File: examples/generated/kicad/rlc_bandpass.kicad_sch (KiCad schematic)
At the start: 5 parts

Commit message: Attempt to create legible symbols.
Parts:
- C1: symbol examples:CAP -> CAP
- L1: symbol examples:INDUCTOR -> INDUCTOR
- R1, R2: symbol examples:R -> R
- V1: symbol examples:VSOURCE -> VSOURCE
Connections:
- net GND: now also C1.1, C1.2, L1.2, R2.1, R2.2, V1.1 (E1)
- new net: R1.1, V1.2 (E2)
- new net: L1.1, R1.2
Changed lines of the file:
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@@
     (comment 1 "Generated by mixedsig2cad")
   )
-  (symbol (lib_id "examples:VSOURCE") (at 50.00 55.00 0) (unit 1)
+  (symbol (lib_id "VSOURCE") (at 50.00 55.00 0) (unit 1)
     (in_bom yes) (on_board yes)
     (property "Reference" "V1" (at 50.0 51.19 0)
@@
     )
   )
-  (symbol (lib_id "examples:R") (at 95.00 55.00 90) (unit 1)
+  (symbol (lib_id "R") (at 95.00 55.00 90) (unit 1)
     (in_bom yes) (on_board yes)
     (property "Reference" "R1" (at 95.0 51.19 0)
@@
     )
   )
-  (symbol (lib_id "examples:INDUCTOR") (at 95.00 90.00 0) (unit 1)
+  (symbol (lib_id "INDUCTOR") (at 95.00 90.00 0) (unit 1)
     (in_bom yes) (on_board yes)
     (property "Reference" "L1" (at 95.0 86.19 0)
@@
     )
   )
-  (symbol (lib_id "examples:CAP") (at 95.00 125.00 90) (unit 1)
+  (symbol (lib_id "CAP") (at 95.00 125.00 90) (unit 1)
     (in_bom yes) (on_board yes)
     (property "Reference" "C1" (at 95.0 121.19 0)
@@
     )
   )
-  (symbol (lib_id "examples:R") (at 95.00 160.00 90) (unit 1)
+  (symbol (lib_id "R") (at 95.00 160.00 90) (unit 1)
     (in_bom yes) (on_board yes)
     (property "Reference" "R2" (at 95.0 156.19 0)
@@
     )
   )
-  (symbol (lib_id "examples:GND") (at 38.00 41.38 0) (unit 1)
+  (symbol (lib_id "GND") (at 38.00 41.38 0) (unit 1)
     (in_bom yes) (on_board yes)
     (property "Reference" "#PWR0001" (at 38.0 37.57 0)

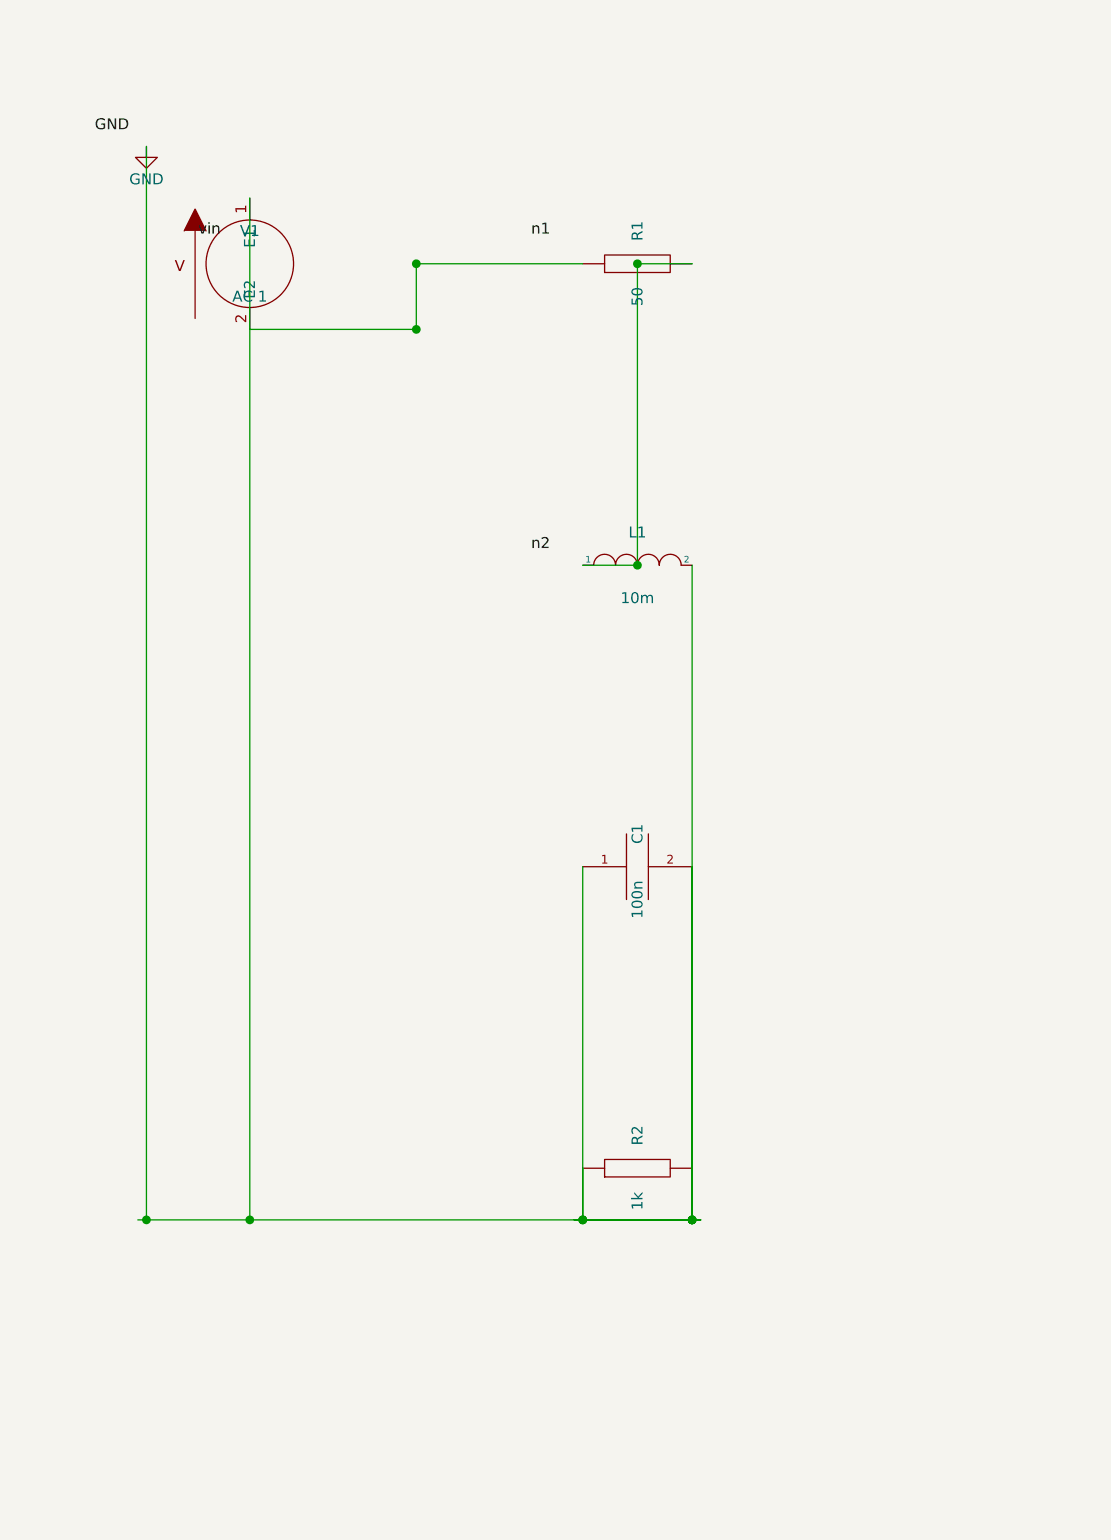
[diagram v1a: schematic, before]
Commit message: Attempt full seperation of circuit concerns into layers.
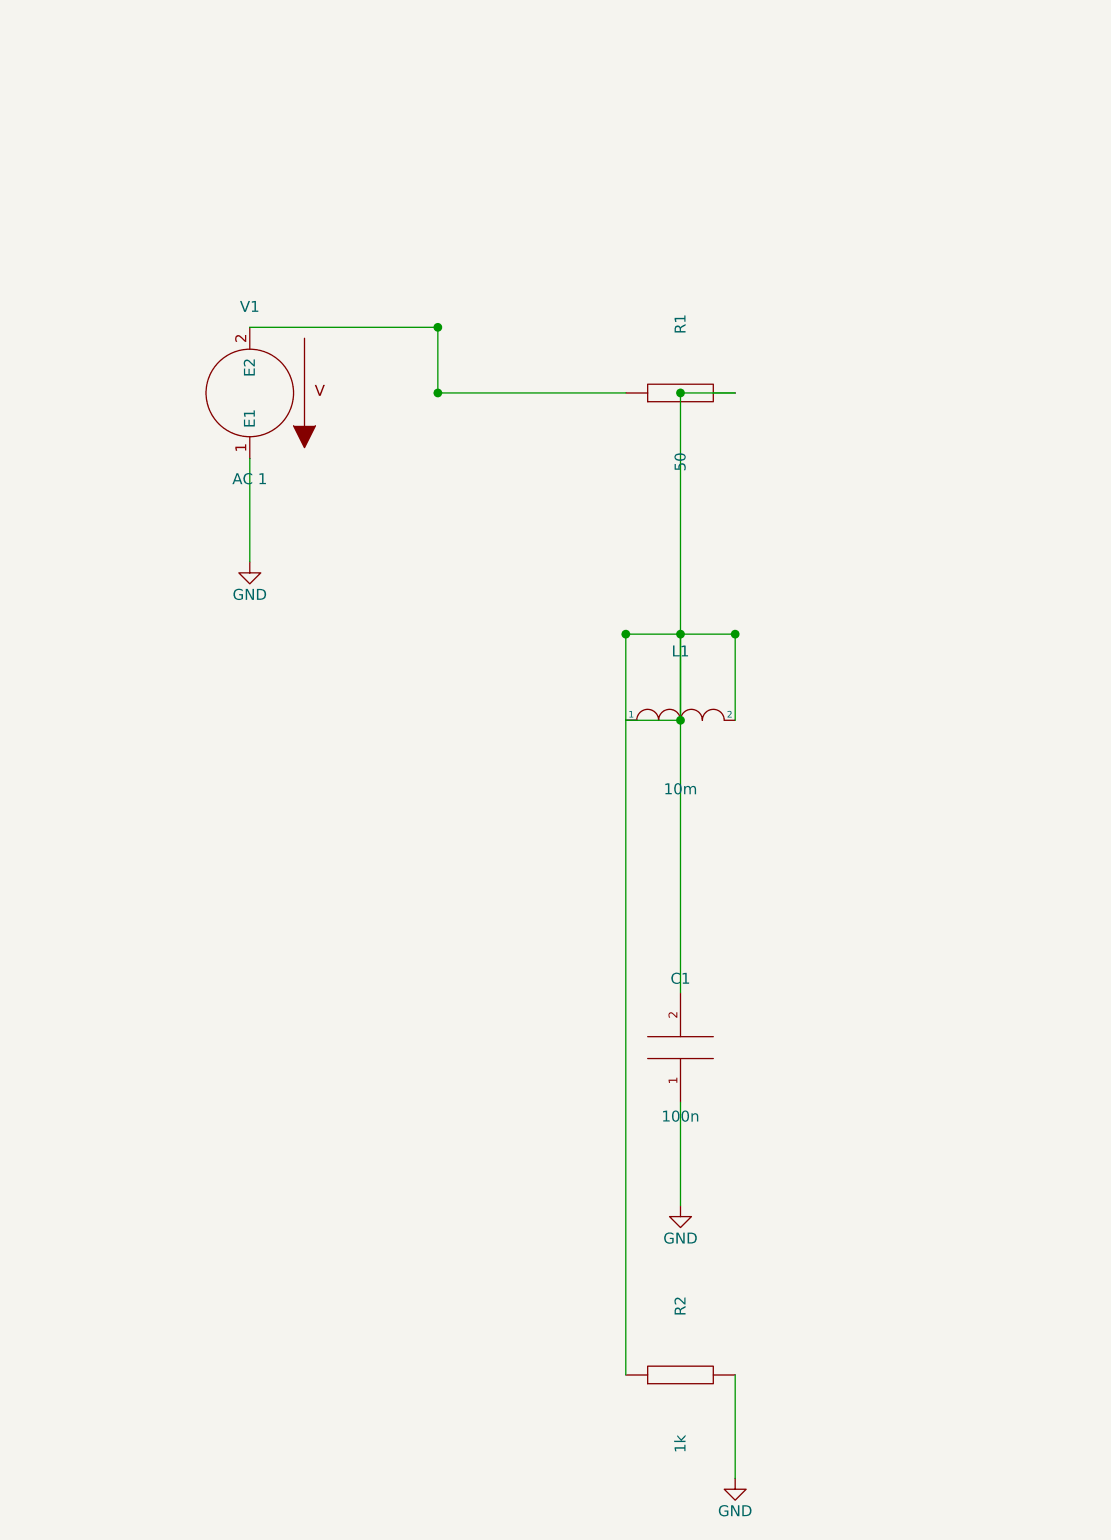
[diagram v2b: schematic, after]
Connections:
- net GND: no longer C1.2, L1.2, R2.1
- net at L1.1, R1.2: now also C1.2, L1.2, R2.1
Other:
- moved on the sheet: C1, L1, R1, R2, V1
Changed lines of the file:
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@@
   (title_block
     (title "rlc_bandpass")
-    (date "2026-03-05")
+    (date "2026-03-06")
     (comment 1 "Generated by mixedsig2cad")
   )
-  (symbol (lib_id "VSOURCE") (at 50.00 55.00 0) (unit 1)
+  (symbol (lib_id "VSOURCE") (at 50.00 70.00 180) (unit 1)
     (in_bom yes) (on_board yes)
-    (property "Reference" "V1" (at 50.0 51.19 0)
+    (property "Reference" "V1" (at 50.0 60.0 0)
       (effects (font (size 1.27 1.27)))
     )
-    (property "Value" "AC 1" (at 50.0 58.81 0)
+    (property "Value" "AC 1" (at 50.0 80.0 0)
       (effects (font (size 1.27 1.27)))
     )
@@
     )
   )
-  (symbol (lib_id "R") (at 95.00 55.00 90) (unit 1)
+  (symbol (lib_id "R") (at 100.00 70.00 90) (unit 1)
     (in_bom yes) (on_board yes)
-    (property "Reference" "R1" (at 95.0 51.19 0)
+    (property "Reference" "R1" (at 100.0 62.0 0)
       (effects (font (size 1.27 1.27)))
     )
-    (property "Value" "50" (at 95.0 58.81 0)
+    (property "Value" "50" (at 100.0 78.0 0)
       (effects (font (size 1.27 1.27)))
     )
@@
     )
   )
-  (symbol (lib_id "INDUCTOR") (at 95.00 90.00 0) (unit 1)
+  (symbol (lib_id "INDUCTOR") (at 100.00 108.00 0) (unit 1)
     (in_bom yes) (on_board yes)
-    (property "Reference" "L1" (at 95.0 86.19 0)
+    (property "Reference" "L1" (at 100.0 100.0 0)
       (effects (font (size 1.27 1.27)))
     )
-    (property "Value" "10m" (at 95.0 93.81 0)
+    (property "Value" "10m" (at 100.0 116.0 0)
       (effects (font (size 1.27 1.27)))
     )
@@
     )
   )
-  (symbol (lib_id "CAP") (at 95.00 125.00 90) (unit 1)
+  (symbol (lib_id "CAP") (at 100.00 146.00 180) (unit 1)
     (in_bom yes) (on_board yes)
-    (property "Reference" "C1" (at 95.0 121.19 0)
+    (property "Reference" "C1" (at 100.0 138.0 0)
       (effects (font (size 1.27 1.27)))
     )
-    (property "Value" "100n" (at 95.0 128.81 0)
+    (property "Value" "100n" (at 100.0 154.0 0)
       (effects (font (size 1.27 1.27)))
     )
@@
     )
   )
-  (symbol (lib_id "R") (at 95.00 160.00 90) (unit 1)
+  (symbol (lib_id "R") (at 100.00 184.00 90) (unit 1)
     (in_bom yes) (on_board yes)
-    (property "Reference" "R2" (at 95.0 156.19 0)
+    (property "Reference" "R2" (at 100.0 176.0 0)
       (effects (font (size 1.27 1.27)))
     )
-    (property "Value" "1k" (at 95.0 163.81 0)
+    (property "Value" "1k" (at 100.0 192.0 0)
       (effects (font (size 1.27 1.27)))
     )
@@
     )
   )
-  (symbol (lib_id "GND") (at 38.00 41.38 0) (unit 1)
+  (symbol (lib_id "GND") (at 50.00 89.62 0) (unit 1)
     (in_bom yes) (on_board yes)
-    (property "Reference" "#PWR0001" (at 38.0 37.57 0)
+    (property "Reference" "#PWR0001" (at 50.0 85.81 0)
       (effects (font (size 1.27 1.27)) hide)
     )
-    (property "Value" "GND" (at 38.0 45.190000000000005 0)
+    (property "Value" "GND" (at 50.0 93.43 0)
       (effects (font (size 1.27 1.27)))
     )
@@
     )
   )
-  (label "GND" (at 32.00 39.88 0)
-    (effects (font (size 1.27 1.27)) (justify left bottom))
+  (symbol (lib_id "GND") (at 100.00 164.35 0) (unit 1)
+    (in_bom yes) (on_board yes)
+    (property "Reference" "#PWR0002" (at 100.0 160.54 0)
+      (effects (font (size 1.27 1.27)) hide)
+    )
+    (property "Value" "GND" (at 100.0 168.16 0)
+      (effects (font (size 1.27 1.27)))
+    )
+    (property "Footprint" "" (at 0 0 0)
+      (effects (font (size 1.27 1.27)) hide)
+    )
+    (property "Datasheet" "" (at 0 0 0)
+      (effects (font (size 1.27 1.27)) hide)
+    )
   )
-  (label "n1" (at 82.65 52.00 0)
-    (effects (font (size 1.27 1.27)) (justify left bottom))
+  (symbol (lib_id "GND") (at 106.35 196.00 0) (unit 1)
+    (in_bom yes) (on_board yes)
+    (property "Reference" "#PWR0003" (at 106.35 192.19 0)
+      (effects (font (size 1.27 1.27)) hide)
+    )
+    (property "Value" "GND" (at 106.35 199.81 0)
+      (effects (font (size 1.27 1.27)))
+    )
+    (property "Footprint" "" (at 0 0 0)
+      (effects (font (size 1.27 1.27)) hide)
+    )
+    (property "Datasheet" "" (at 0 0 0)
+      (effects (font (size 1.27 1.27)) hide)
+    )
   )
-  (label "n2" (at 82.65 88.50 0)
-    (effects (font (size 1.27 1.27)) (justify left bottom))
-  )
-  (label "vin" (at 44.00 52.00 0)
-    (effects (font (size 1.27 1.27)) (justify left bottom))
-  )
-  (wire (pts (xy 37.00 166.00) (xy 102.35 166.00))
+  (wire (pts (xy 50.00 77.62) (xy 50.00 89.62))
     (stroke (width 0) (type solid) (color 0 0 0 0))
   )
-  (wire (pts (xy 50.00 47.38) (xy 50.00 166.00))
+  (wire (pts (xy 100.00 152.35) (xy 100.00 164.35))
     (stroke (width 0) (type solid) (color 0 0 0 0))
   )
-  (wire (pts (xy 101.35 125.00) (xy 101.35 166.00))
+  (wire (pts (xy 106.35 184.00) (xy 106.35 196.00))
     (stroke (width 0) (type solid) (color 0 0 0 0))
   )
-  (wire (pts (xy 101.35 160.00) (xy 101.35 166.00))
+  (wire (pts (xy 106.35 70.00) (xy 100.00 70.00))
     (stroke (width 0) (type solid) (color 0 0 0 0))
   )
-  (wire (pts (xy 38.00 41.38) (xy 38.00 166.00))
+  (wire (pts (xy 100.00 70.00) (xy 100.00 108.00))
     (stroke (width 0) (type solid) (color 0 0 0 0))
   )
-  (wire (pts (xy 101.35 55.00) (xy 95.00 55.00))
+  (wire (pts (xy 100.00 108.00) (xy 93.65 108.00))
     (stroke (width 0) (type solid) (color 0 0 0 0))
   )
-  (wire (pts (xy 95.00 55.00) (xy 95.00 90.00))
+  (wire (pts (xy 93.65 98.00) (xy 106.35 98.00))
     (stroke (width 0) (type solid) (color 0 0 0 0))
   )
-  (wire (pts (xy 95.00 90.00) (xy 88.65 90.00))
+  (wire (pts (xy 106.35 108.00) (xy 106.35 98.00))
     (stroke (width 0) (type solid) (color 0 0 0 0))
   )
-  (wire (pts (xy 87.65 166.00) (xy 102.35 166.00))
+  (wire (pts (xy 100.00 139.65) (xy 100.00 98.00))
     (stroke (width 0) (type solid) (color 0 0 0 0))
   )
-  (wire (pts (xy 101.35 90.00) (xy 101.35 166.00))
+  (wire (pts (xy 93.65 184.00) (xy 93.65 98.00))
     (stroke (width 0) (type solid) (color 0 0 0 0))
   )
-  (wire (pts (xy 88.65 125.00) (xy 88.65 166.00))
+  (wire (pts (xy 50.00 62.38) (xy 71.83 62.38))
     (stroke (width 0) (type solid) (color 0 0 0 0))
   )
-  (wire (pts (xy 88.65 160.00) (xy 88.65 166.00))
+  (wire (pts (xy 71.83 62.38) (xy 71.83 70.00))
     (stroke (width 0) (type solid) (color 0 0 0 0))
   )
-  (wire (pts (xy 50.00 62.62) (xy 69.33 62.62))
+  (wire (pts (xy 71.83 70.00) (xy 93.65 70.00))
     (stroke (width 0) (type solid) (color 0 0 0 0))
   )
-  (wire (pts (xy 69.33 62.62) (xy 69.33 55.00))
-    (stroke (width 0) (type solid) (color 0 0 0 0))
-  )
-  (wire (pts (xy 69.33 55.00) (xy 88.65 55.00))
-    (stroke (width 0) (type solid) (color 0 0 0 0))
-  )
-  (junction (at 50.00 166.00) (diameter 1.016) (color 0 0 0 0))
-  (junction (at 101.35 166.00) (diameter 1.016) (color 0 0 0 0))
-  (junction (at 101.35 166.00) (diameter 1.016) (color 0 0 0 0))
-  (junction (at 38.00 166.00) (diameter 1.016) (color 0 0 0 0))
-  (junction (at 95.00 55.00) (diameter 1.016) (color 0 0 0 0))
-  (junction (at 95.00 90.00) (diameter 1.016) (color 0 0 0 0))
-  (junction (at 101.35 166.00) (diameter 1.016) (color 0 0 0 0))
-  (junction (at 88.65 166.00) (diameter 1.016) (color 0 0 0 0))
-  (junction (at 88.65 166.00) (diameter 1.016) (color 0 0 0 0))
-  (junction (at 69.33 62.62) (diameter 1.016) (color 0 0 0 0))
-  (junction (at 69.33 55.00) (diameter 1.016) (color 0 0 0 0))
+  (junction (at 100.00 70.00) (diameter 1.016) (color 0 0 0 0))
+  (junction (at 100.00 108.00) (diameter 1.016) (color 0 0 0 0))
+  (junction (at 106.35 98.00) (diameter 1.016) (color 0 0 0 0))
+  (junction (at 100.00 98.00) (diameter 1.016) (color 0 0 0 0))
+  (junction (at 93.65 98.00) (diameter 1.016) (color 0 0 0 0))
+  (junction (at 71.83 62.38) (diameter 1.016) (color 0 0 0 0))
+  (junction (at 71.83 70.00) (diameter 1.016) (color 0 0 0 0))
   (sheet_instances
     (path "/" (page "1"))
@@
     (path "/cd1f9510-5b53-5cd9-9b95-17115dad0ad7" (reference "C1") (unit 1) (value "100n") (footprint ""))
     (path "/b1d9c617-2a8f-5ec8-b477-3e4c80c09fda" (reference "R2") (unit 1) (value "1k") (footprint ""))
-    (path "/07e873c6-1a42-5142-9ed4-09edf6dd5f6f" (reference "#PWR0001") (unit 1) (value "GND") (footprint ""))
+    (path "/377a3052-07db-5d7e-aabd-1d809c76f718" (reference "#PWR0001") (unit 1) (value "GND") (footprint ""))
+    (path "/73773ef2-52e2-515f-9193-ba4c4c232fbe" (reference "#PWR0002") (unit 1) (value "GND") (footprint ""))
+    (path "/031d87f3-084d-5a64-83f1-7b1a54b82eb9" (reference "#PWR0003") (unit 1) (value "GND") (footprint ""))
   )
 )

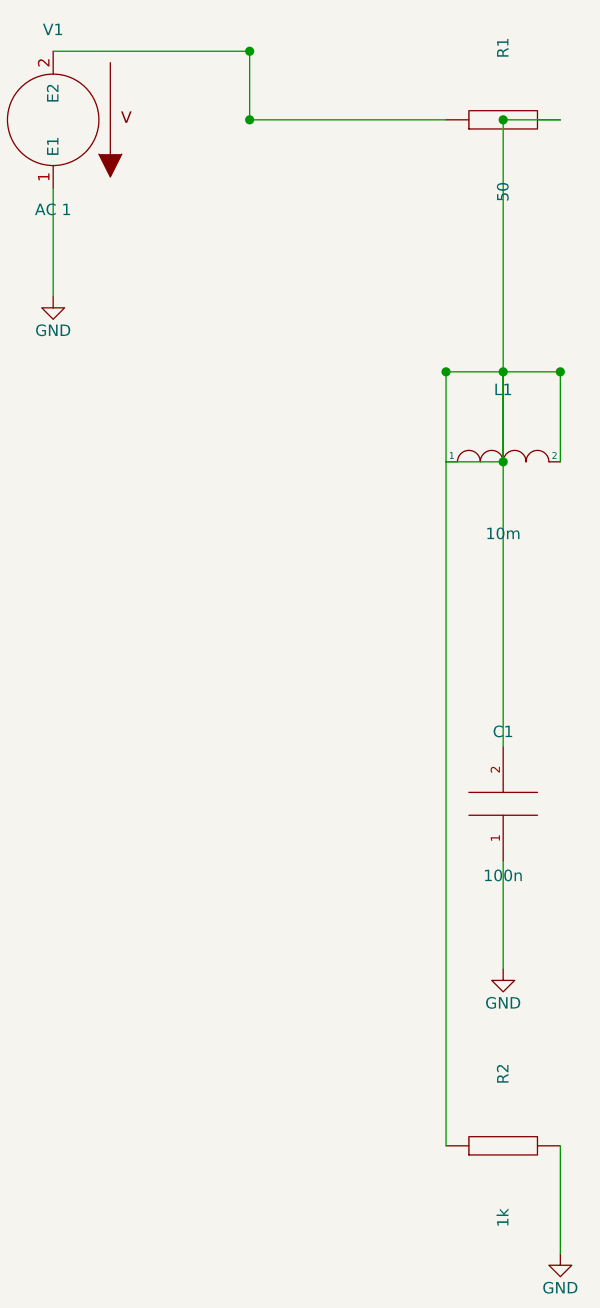
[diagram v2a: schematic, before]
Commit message: Add checks for connectivity.
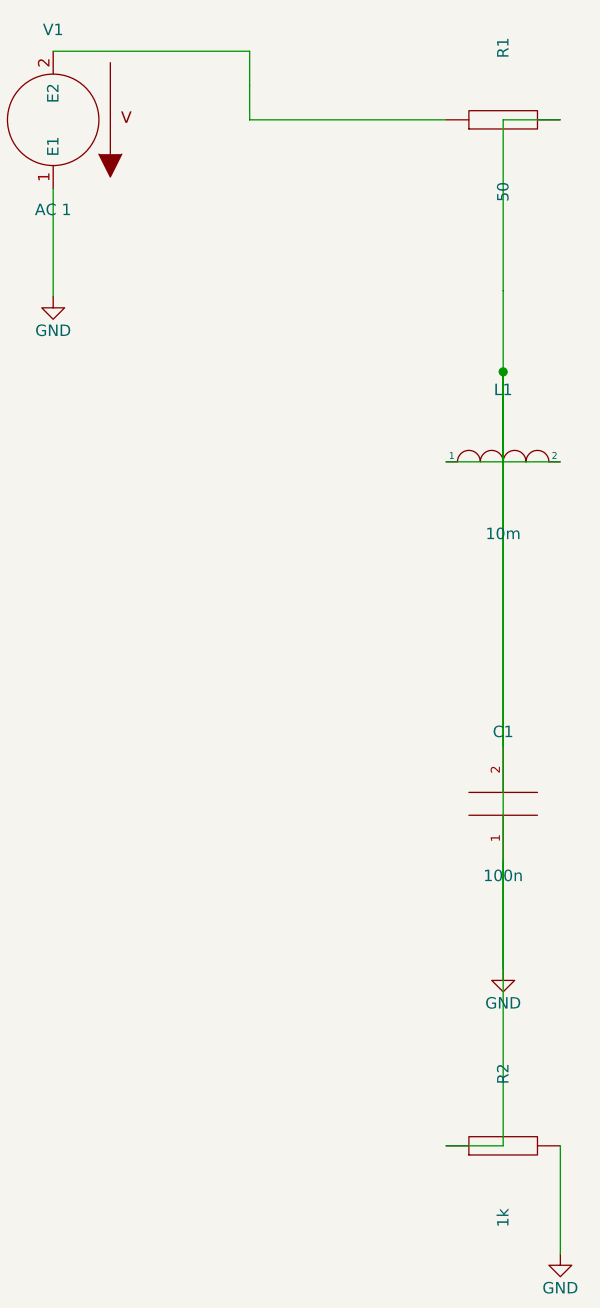
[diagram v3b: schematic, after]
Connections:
- net GND: now also C1.2, L1.1, L1.2, R1.2, R2.1
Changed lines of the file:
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@@
     (stroke (width 0) (type solid) (color 0 0 0 0))
   )
-  (wire (pts (xy 100.00 70.00) (xy 100.00 108.00))
+  (wire (pts (xy 100.00 70.00) (xy 100.00 89.00))
     (stroke (width 0) (type solid) (color 0 0 0 0))
   )
-  (wire (pts (xy 100.00 108.00) (xy 93.65 108.00))
+  (wire (pts (xy 93.65 108.00) (xy 100.00 108.00))
     (stroke (width 0) (type solid) (color 0 0 0 0))
   )
-  (wire (pts (xy 93.65 98.00) (xy 106.35 98.00))
+  (wire (pts (xy 100.00 108.00) (xy 100.00 89.00))
     (stroke (width 0) (type solid) (color 0 0 0 0))
   )
-  (wire (pts (xy 106.35 108.00) (xy 106.35 98.00))
+  (wire (pts (xy 106.35 108.00) (xy 100.00 108.00))
+    (stroke (width 0) (type solid) (color 0 0 0 0))
+  )
+  (wire (pts (xy 100.00 108.00) (xy 100.00 98.00))
     (stroke (width 0) (type solid) (color 0 0 0 0))
   )
@@
     (stroke (width 0) (type solid) (color 0 0 0 0))
   )
-  (wire (pts (xy 93.65 184.00) (xy 93.65 98.00))
+  (wire (pts (xy 93.65 184.00) (xy 100.00 184.00))
+    (stroke (width 0) (type solid) (color 0 0 0 0))
+  )
+  (wire (pts (xy 100.00 184.00) (xy 100.00 98.00))
     (stroke (width 0) (type solid) (color 0 0 0 0))
   )
@@
     (stroke (width 0) (type solid) (color 0 0 0 0))
   )
-  (wire (pts (xy 71.83 62.38) (xy 71.83 70.00))
+  (wire (pts (xy 71.83 62.38) (xy 71.83 66.19))
     (stroke (width 0) (type solid) (color 0 0 0 0))
   )
-  (wire (pts (xy 71.83 70.00) (xy 93.65 70.00))
+  (wire (pts (xy 93.65 70.00) (xy 71.83 70.00))
     (stroke (width 0) (type solid) (color 0 0 0 0))
   )
-  (junction (at 100.00 70.00) (diameter 1.016) (color 0 0 0 0))
-  (junction (at 100.00 108.00) (diameter 1.016) (color 0 0 0 0))
-  (junction (at 106.35 98.00) (diameter 1.016) (color 0 0 0 0))
+  (wire (pts (xy 71.83 70.00) (xy 71.83 66.19))
+    (stroke (width 0) (type solid) (color 0 0 0 0))
+  )
   (junction (at 100.00 98.00) (diameter 1.016) (color 0 0 0 0))
-  (junction (at 93.65 98.00) (diameter 1.016) (color 0 0 0 0))
-  (junction (at 71.83 62.38) (diameter 1.016) (color 0 0 0 0))
-  (junction (at 71.83 70.00) (diameter 1.016) (color 0 0 0 0))
   (sheet_instances
     (path "/" (page "1"))
